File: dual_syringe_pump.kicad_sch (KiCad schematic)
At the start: 45 parts, among them J1 USB_C_Receptacle_USB2.0_16P, Q1 SS8050, Q2 SS8050, SW1 boot, SW2 reset, U1 AMS1117-3.3, U2 ESP32-WROOM-32, U3 CH340C

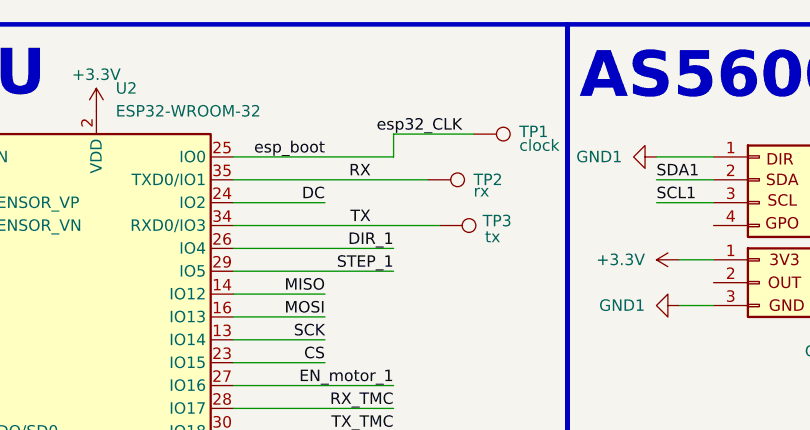
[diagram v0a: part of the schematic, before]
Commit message: changed to mouse bites
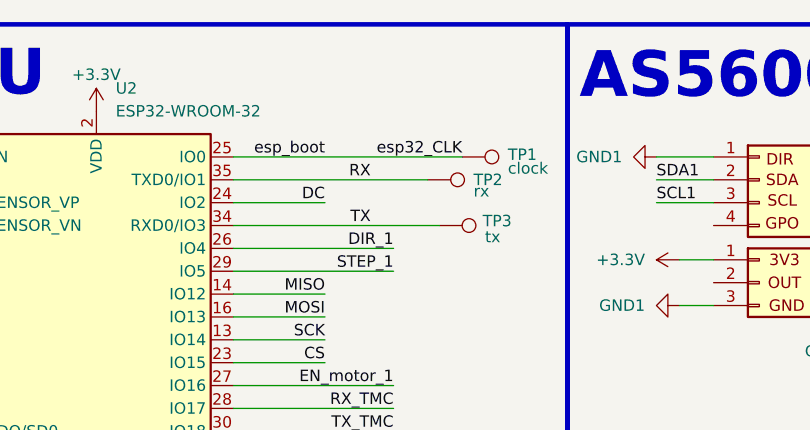
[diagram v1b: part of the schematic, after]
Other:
- moved on the sheet: TP1
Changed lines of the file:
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@@
 	(wire
 		(pts
-			(xy 68.58 24.13) (xy 77.47 24.13)
-		)
-		(stroke
-			(width 0)
-			(type default)
-		)
-	)
-	(wire
-		(pts
 			(xy 242.57 139.7) (xy 246.38 139.7)
 		)
@@
 	(wire
 		(pts
-			(xy 68.58 26.67) (xy 50.8 26.67)
+			(xy 50.8 26.67) (xy 76.2 26.67)
 		)
 		(stroke
@@
 	(wire
 		(pts
-			(xy 68.58 24.13) (xy 68.58 26.67)
-		)
-		(stroke
-			(width 0)
-			(type default)
-		)
-	)
-	(wire
-		(pts
 			(xy 43.18 140.97) (xy 49.53 140.97)
 		)
@@
 	)
 	(label "esp32_CLK"
-		(at 76.2 24.13 180)
+		(at 76.2 26.67 180)
 		(effects
 			(font
@@
 	(symbol
 		(lib_id "Connector:TestPoint")
-		(at 77.47 24.13 270)
+		(at 76.2 26.67 270)
 		(unit 1)
 		(exclude_from_sim no)
@@
 		(dnp no)
 		(property "Reference" "TP1"
-			(at 82.55 23.876 90)
+			(at 81.28 26.416 90)
 			(effects
 				(font
@@
 		)
 		(property "Value" "clock"
-			(at 82.55 25.3999 90)
+			(at 81.28 27.9399 90)
 			(effects
 				(font
@@
 		)
 		(property "Footprint" "TestPoint:TestPoint_Pad_D1.0mm"
-			(at 77.47 29.21 0)
+			(at 76.2 31.75 0)
 			(effects
 				(font
@@
 		)
 		(property "Datasheet" "~"
-			(at 77.47 29.21 0)
+			(at 76.2 31.75 0)
 			(effects
 				(font
@@
 		)
 		(property "Description" "test point"
-			(at 77.47 24.13 0)
+			(at 76.2 26.67 0)
 			(effects
 				(font

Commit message: post production fixes
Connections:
- net bat% is gone; now on net V_bat%: U2.37 (IO23)
- net GND1: now also bat_%1.1 (Pin_1)
- net V_bat%: now reaches bat_%1.2 (Pin_2)
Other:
- note added: "Stepper driver"
- note added: "Test Points"
- note added: "a"
- note added: "b"
- note added: "c"
- note added: "d"
- note added: "e"
- note added: "f"
- note added: "g"
- note added: "h"
- note removed: "Stepper"
- moved on the sheet: 3V1, C11, C4, C5, C6, C7, C8, C9, EN_BOT_1, EN_BOT_2, EN_TOP_1, EN_TOP_2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
